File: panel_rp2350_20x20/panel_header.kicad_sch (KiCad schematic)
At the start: 4 parts, among them J2 Conn_01x05, J3 Conn_01x05, J4 Conn_01x05, J5 Conn_01x05

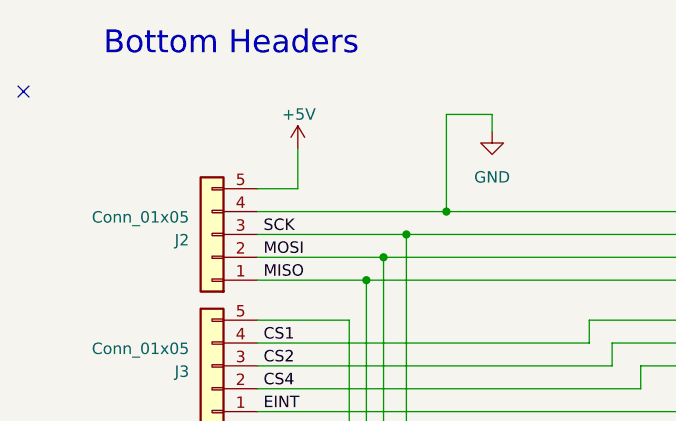
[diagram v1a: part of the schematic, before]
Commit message: Worked on rp2350 20x20 panel layout and routing.
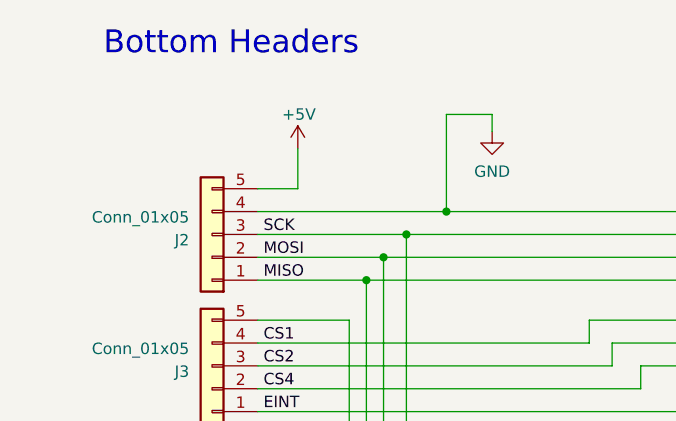
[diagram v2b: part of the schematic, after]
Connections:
- no-connect marks 2 -> 1
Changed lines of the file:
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@@
-	)
-	(no_connect
-		(at 78.74 74.93)
 	)
 	(no_connect
@@
 		)
 		(property "Value" "GND"
-			(at 130.81 84.455 0)
-			(effects
-				(font
+			(at 130.81 83.82 0)
+			(effects
+				(font

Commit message: Renamed to panel_rp2354_20x20. Creaetd inition production files.
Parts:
- J4, J5: LCSC Part # (none) -> C21116902
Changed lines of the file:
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@@
+			)
+		)
+		(property "LCSC Part #" "C21116902 "
+			(at 179.07 105.41 0)
+			(effects
+				(font
+					(size 1.27 1.27)
+				)
+				(hide yes)
 			)
 		)
@@
 			)
 		)
+		(property "LCSC Part #" "C21116902 "
+			(at 179.07 90.805 0)
+			(effects
+				(font
+					(size 1.27 1.27)
+				)
+				(hide yes)
+			)
+		)
